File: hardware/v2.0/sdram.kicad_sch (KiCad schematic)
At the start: 10 parts, among them IC1 IS42S16160J-6BLI, U1 ECP5U-25F-CABGA256

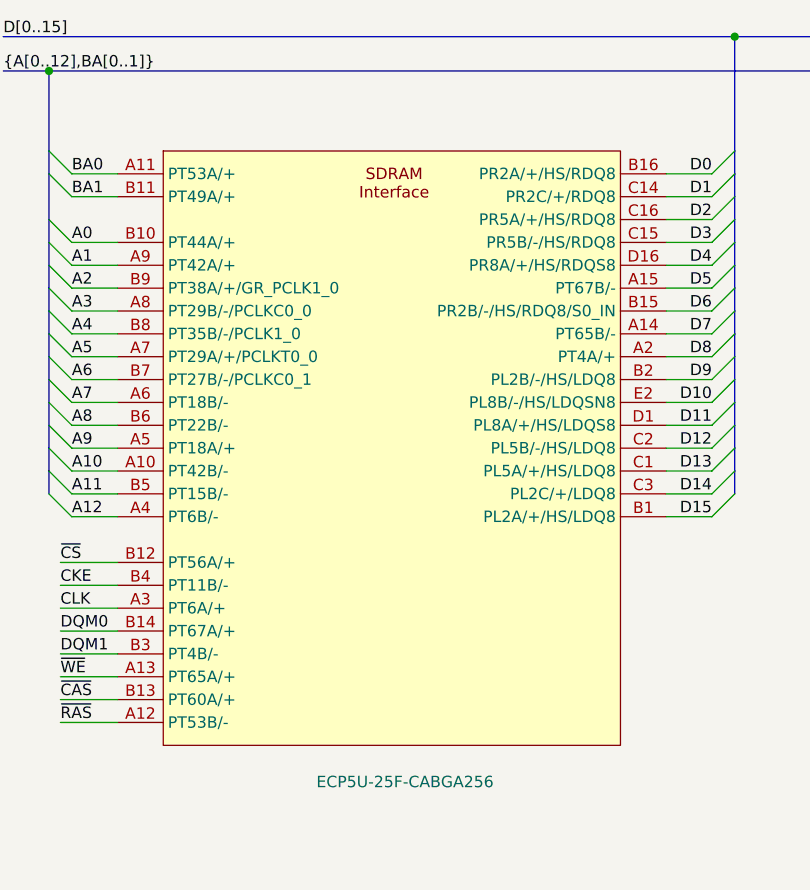
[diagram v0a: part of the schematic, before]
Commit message: ADC 6 diff lines
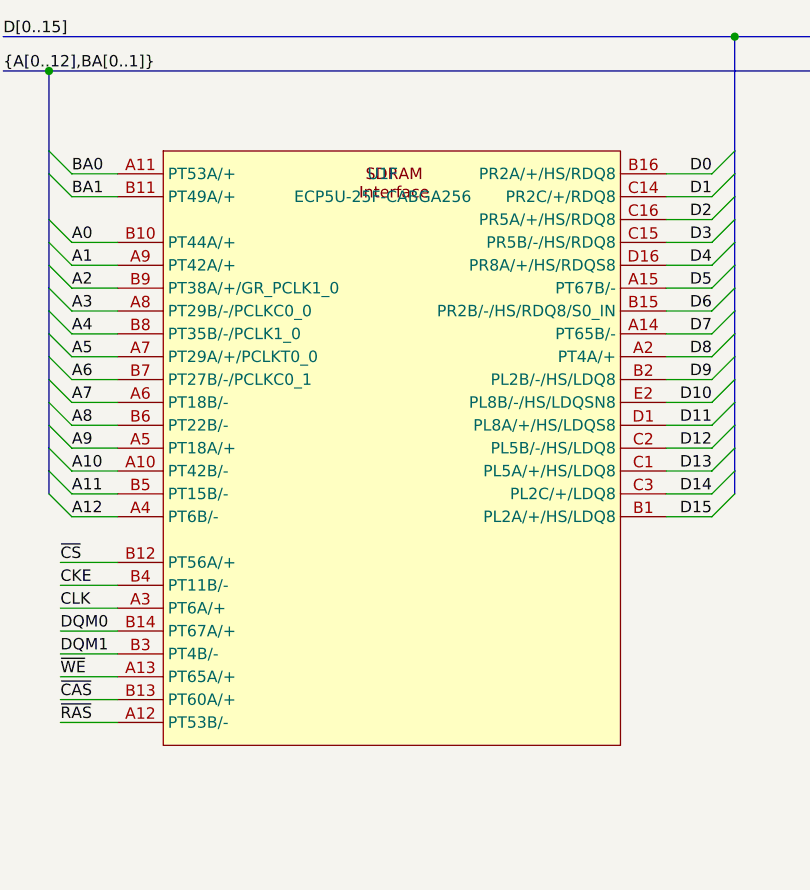
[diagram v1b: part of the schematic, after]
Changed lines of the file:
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@@
 		(dnp no)
 		(property "Reference" "U1"
-			(at 89.662 32.512 0)
+			(at 90.424 69.85 0)
 			(effects
 				(font
 					(size 1.27 1.27)
 				)
-				(hide yes)
 			)
 		)
 		(property "Value" "ECP5U-25F-CABGA256"
-			(at 83.058 137.414 0)
+			(at 90.424 72.39 0)
 			(effects
 				(font
 					(size 1.27 1.27)
 				)
-				(justify left)
 			)
 		)
@@
 					(reference "U1")
 					(unit 6)
+				)
+				(path "/f88da08e-cf42-4d03-a08f-3f602fe6658d/b5a9aa02-311b-4a9a-a7d4-646f15cdd9c2"
+					(reference "U1")
+					(unit 6)

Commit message: ADC CLKOUT±
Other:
- company: Chengyin Yao (cheyao), Vadym Vikulin -> Vadym Vikulin, Chengyin Yao (cheyao)
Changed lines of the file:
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@@
 	(title_block
 		(title "Icepi Zero")
-		(date "2026-01-05")
-		(rev "v2.0")
-		(company "Chengyin Yao (cheyao), Vadym Vikulin")
-		(comment 1 "https://github.com/cheyao/icepi-zero")
+		(date "2026-01-17")
+		(rev "v2.1")
+		(company "Vadym Vikulin, Chengyin Yao (cheyao)")
+		(comment 1 "https://github.com/vikulin/icepi-zero")
 		(comment 2 "License: Solderpad")
 		(comment 9 "OSHWA FR000026")
@@
 		(pin "P11"
 		)
+		(pin "N6"
+		)
 		(instances

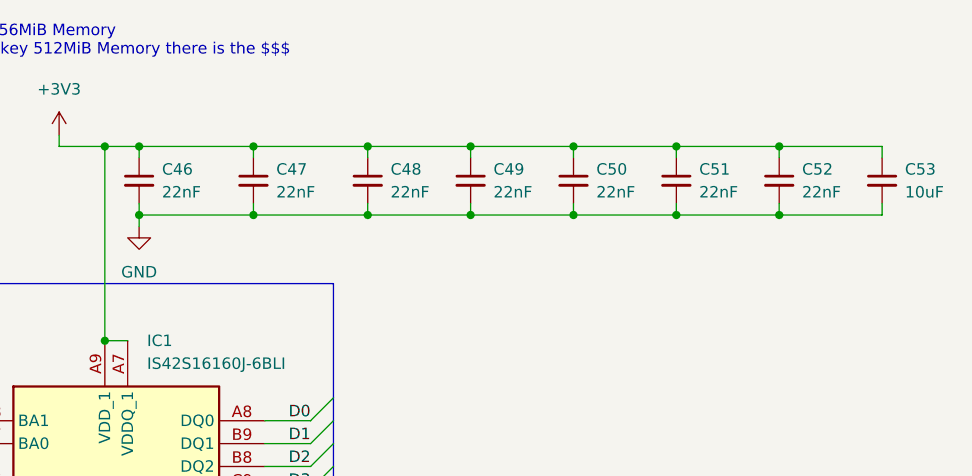
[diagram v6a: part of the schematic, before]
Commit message: BOM fields unification for PCBWay requirements
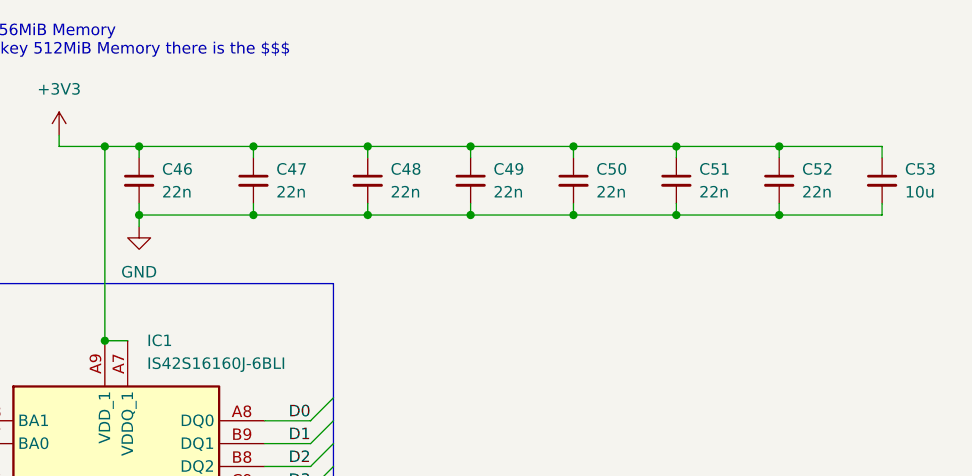
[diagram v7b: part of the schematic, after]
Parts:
- C46, C47, C48, C50, C51, C52: value 22nF -> 22n; MANUFACTURER (none) -> FH; MANUFACTURER_PART_NUMBER (none) -> 0603B223K500NT
- C49: value 22nF -> 22n; LCSC Link https://lcsc.com/product-detail/Multilayer-Ceramic-Capacito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 -> https://www.lcsc.com/product-detail/C77571.html; MANUFACTURER (none) -> FH; MANUFACTURER_PART_NUMBER (none) -> 0603B223K500NT
- C53: value 10uF -> 10u; MANUFACTURER (none) -> Samsung Electro-Mechanics; MANUFACTURER_PART_NUMBER (none) -> CL10A106KP8NNNC
- IC1: MANUFACTURER (none) -> ISSI; MANUFACTURER_PART_NUMBER (none) -> IS42S16160J-6BLI
- U1: MANUFACTURER (none) -> Lattice; MANUFACTURER_PART_NUMBER (none) -> LFE5U-25F-6BG256C
